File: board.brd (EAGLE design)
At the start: 126.7 x 85.7 mm, 192 parts, among them J1 XEM6310, U1 AD8022ARMZ, U2 AD5754BREZ, U3 ADR420ARZ, U4 LT1175CS8-5PBF, U5 LT1763CS8-5PBF, U6 AD5754BREZ, U7 ADR420ARZ, U8 AD8022ARMZ, U9 AD8022ARMZ, X1 LTI-SASF54GT, X10 LTI-SASF54GT, X11 LTI-SASF54GT, X12 LTI-SASF54GT, X13 LTI-SASF54GT, X14 LTI-SASF54GT, X2 LTI-SASF54GT, X3 LTI-SASF54GT, X4 LTI-SASF54GT, X5 LTI-SASF54GT, X6 LTI-SASF54GT, X7 LTI-SASF54GT, X8 LTI-SASF54GT, X9 LTI-SASF54GT

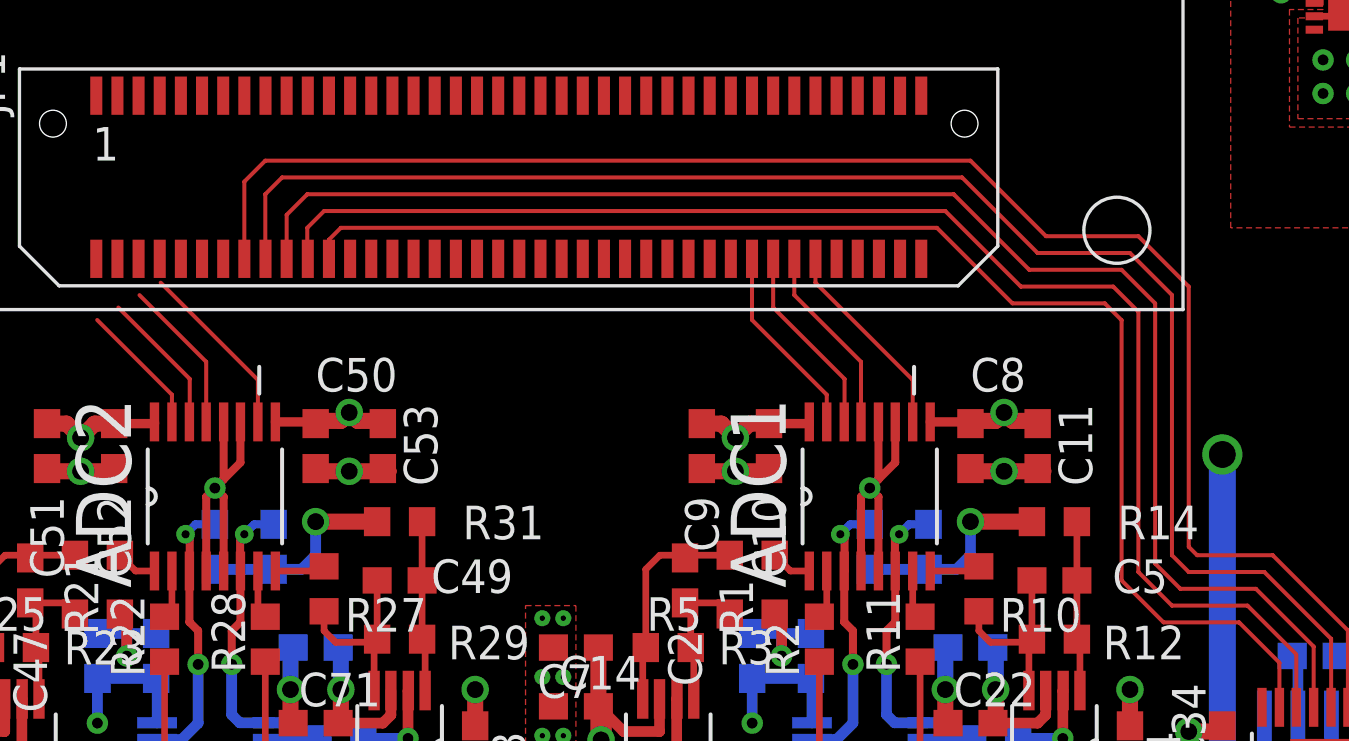
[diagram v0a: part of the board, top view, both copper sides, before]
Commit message: Board/schematic consistency
Need input wiring now
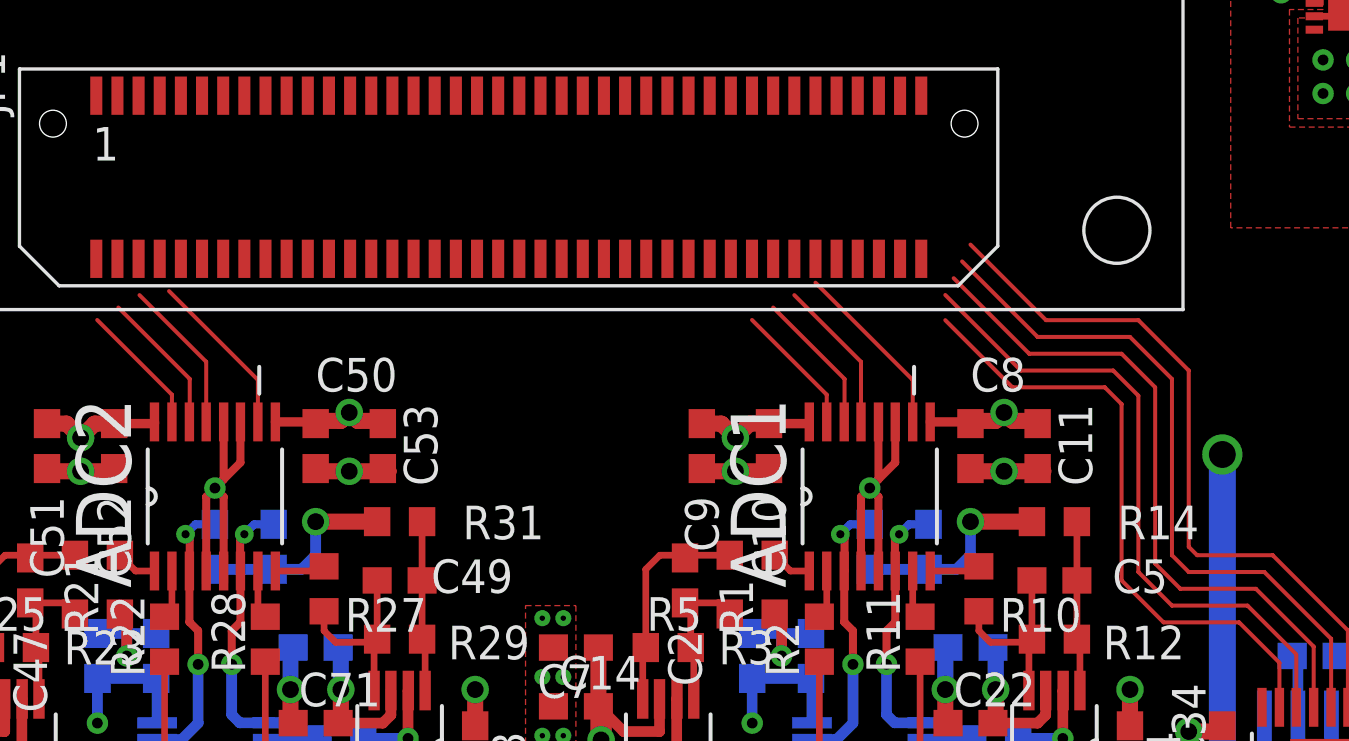
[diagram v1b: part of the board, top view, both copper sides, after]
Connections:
- net VREF1A1 renamed VREF2A
- net VREF1A2 renamed VREF3A
- net VREF1B1 renamed VREF2B
- net VREF1B2 renamed VREF3B
- removed net ADC4: J1.272
- removed net ADC5: J1.274
- removed net ADC6: J1.276
- removed net EP1: U6.25
- net ADC0: now also J1.266; no longer J1.270
- net ADC1: now also J1.264; no longer J1.268
- net ADC2: now also J1.262; no longer J1.266
- net ADC3: now also J1.260; no longer J1.264
- net DACD0: now also J1.268; no longer J1.216
- net DACD1: now also J1.270; no longer J1.218
- net DACD2: now also J1.274; no longer J1.222
- net DACD3: now also J1.272; no longer J1.220
- net DACD4: now also J1.276; no longer J1.224
- net EP: now also U6.25
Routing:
- net DACD0: track 61.0 -> 27.1 mm
- net DACD1: track 58.6 -> 26.4 mm
- net DACD3: track 56.0 -> 25.6 mm
- net DACD2: track 53.6 -> 24.8 mm
- net DACD4: track 51.1 -> 23.6 mm
- net ADC3: track 7.34 -> 5.03 mm
- net ADC2: track 7.29 -> 5.45 mm
- net ADC1: track 7.21 -> 5.84 mm
- net ADC0: track 7.69 -> 6.79 mm

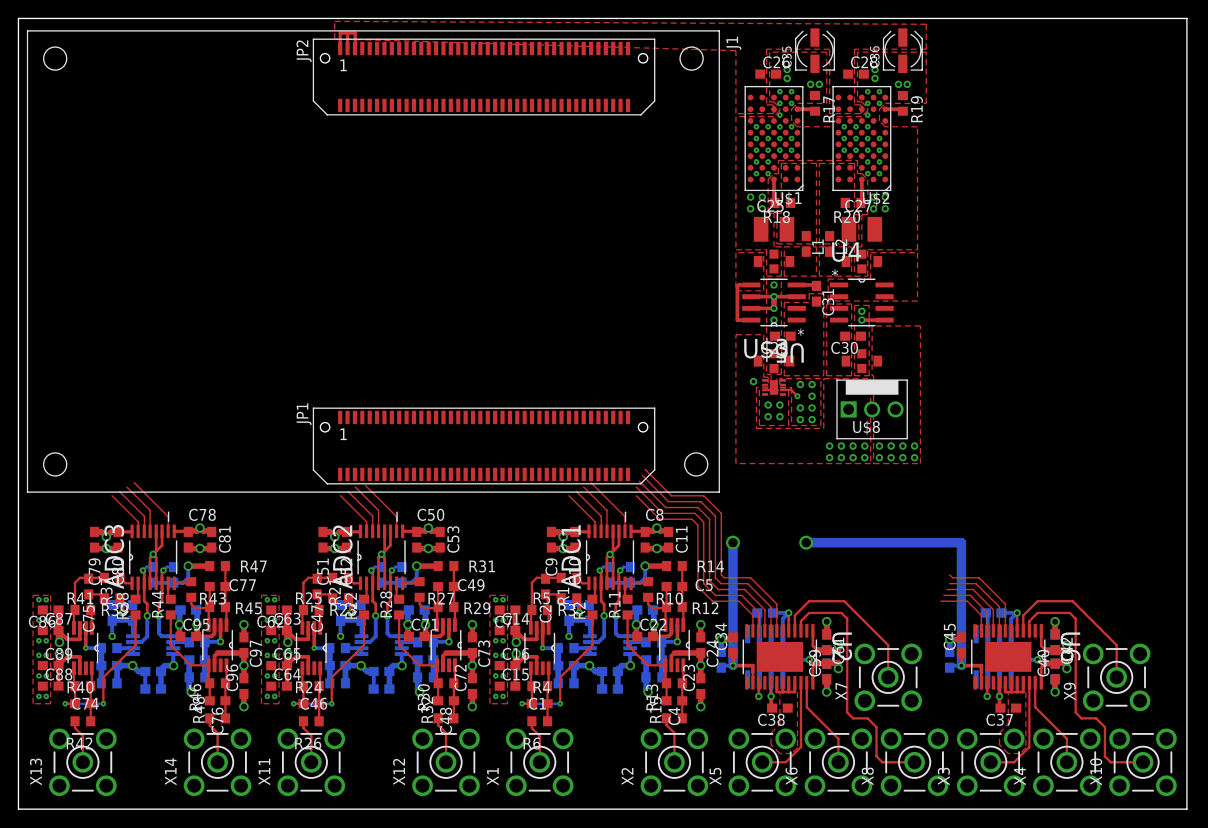
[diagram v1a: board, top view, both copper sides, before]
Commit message: Routed signals
Need to fix SMA connector spacing
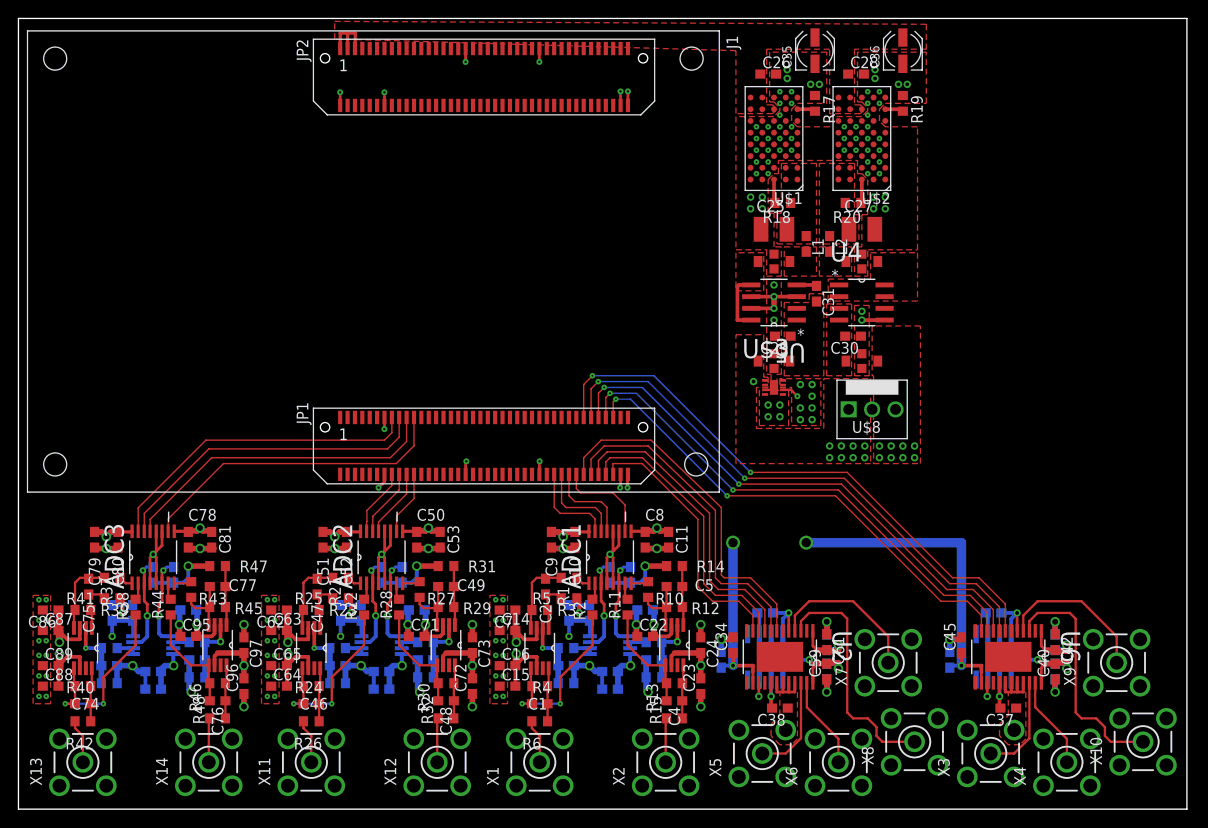
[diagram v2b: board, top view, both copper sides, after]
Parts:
- moved X10 2.22 mm to (121.9, 7.30)
- moved X8 2.22 mm to (97.2, 7.30)
- moved X7 1.59 mm to (94.3, 15.9)
- moved X9 1.59 mm to (119.1, 15.9)
- moved X14 0.95 mm to (20.6, 5.08)
- moved X2 0.95 mm to (70.2, 5.08)
- moved X3 0.95 mm to (105.4, 6.03)
- moved X5 0.95 mm to (80.6, 6.03)
- moved X12 0.95 mm to (45.4, 5.08)
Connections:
- removed net EP: U2.25, U6.25
- new net N$94: U6.25
- new net N$95: U2.25
- net ADC10: now also J1.216
- net ADC11: now also J1.221
- net ADC12: now also J1.219
- net ADC13: now also J1.217
- net ADC14: now also J1.215
- net ADC7: now also J1.222
- net ADC8: now also J1.220
- net ADC9: now also J1.218
- net DACD2: now also J1.272, U2.9; no longer J1.274, U2.10
- net DACD3: now also J1.274, U2.10; no longer J1.272, U2.9
- net DACD5: now also J1.267, U6.7; no longer U6.8
- net DACD6: now also J1.269, U6.8; no longer U6.10
- net DACD7: now also J1.271
- net DACD8: now also J1.273, U6.10; no longer U6.11
- net DACD9: now also J1.275, U6.11; no longer U6.7
- net GND: now also J1.102, J1.114, J1.135, J1.155, J1.178, J1.180, J1.213, J1.214, J1.236, J1.256, J1.278, J1.280
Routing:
- net DACD5: track 9.02 -> 62.8 mm, vias 0 -> 2
- net DACD6: track 7.47 -> 60.4 mm, vias 0 -> 2
- net DACD7: track 8.25 -> 58.0 mm, vias 0 -> 2
- net DACD8: track 6.70 -> 55.5 mm, vias 0 -> 2
- net DACD9: track 10.2 -> 53.1 mm, vias 0 -> 2
- net ADC14: track 5.03 -> 35.1 mm
- net ADC13: track 5.45 -> 35.1 mm
- net ADC12: track 5.84 -> 35.2 mm
- net ADC11: track 6.79 -> 34.4 mm
- net GND: track 197.2 -> 214.7 mm, vias 139 -> 151
- net DACD0: track 27.1 -> 38.0 mm
- net DACD1: track 26.4 -> 35.8 mm
- net DACD2: track 24.8 -> 33.5 mm
- net DACD3: track 25.6 -> 31.3 mm
- net DACD4: track 23.6 -> 29.1 mm
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
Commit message: Fixed power
Added caps for all linear regulators
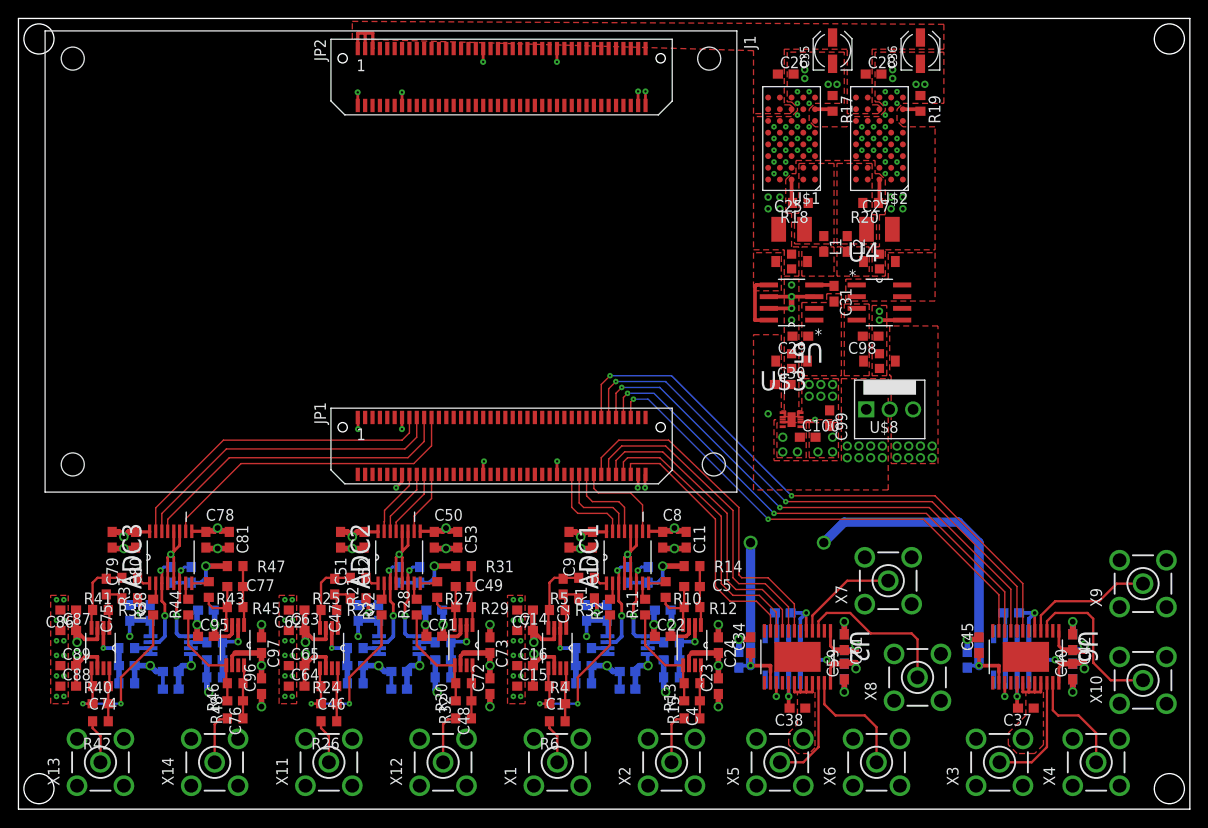
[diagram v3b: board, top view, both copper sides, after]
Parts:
- added C100, C99: 4.7uF, rcl:C0603
- added C98: 1uF Tant, rcl:C0603T
- C30: value 0.1uF Tant -> 4.7uF
- C35, C36: value (none) -> 100uF
- moved C30 9.25 mm to (82.9, 46.0), turned to 0 degrees
- moved X9 9.04 mm to (121.9, 24.4)
- moved X7 8.89 mm to (94.3, 24.8)
- moved X8 6.99 mm to (97.5, 14.3)
- moved X10 6.67 mm to (121.9, 14.0)
- moved X6 4.13 mm to (93.0, 5.08)
- moved U$3 3.98 mm to (83.8, 42.2)
- moved X4 3.17 mm to (116.8, 5.08)
- moved X5 2.13 mm to (82.5, 5.08)
- moved R2 1.91 mm to (64.1, 21.9)
- moved ADC1 1.91 mm to (66.0, 27.3)
- moved ADC2 1.91 mm to (41.3, 27.3)
- moved ADC3 1.91 mm to (16.5, 27.3)
- moved ADCOP1 1.91 mm to (58.4, 17.5)
- moved ADCOP2 1.91 mm to (73.0, 17.8)
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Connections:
- net +3V3: now also C99.1
- net +5V: now also C30.1
- net GND: now also C100.2, C30.2, C98.+, C99.2, J1.201; no longer C30.1
- net N$66: now also C98.-; no longer C30.2
- net VDD: now also C100.1
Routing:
- net N$39: track 32.4 -> 42.7 mm
- net N$21: track 26.0 -> 17.5 mm
- net N$45: track 26.0 -> 17.7 mm
- net N$18: track 16.9 -> 11.4 mm
- net N$40: track 10.8 -> 13.8 mm
- net N$28: track 1.11 -> 4.13 mm
- net S$1: track 21.2 -> 24.0 mm
- net N$19: track 10.0 -> 12.8 mm
- net N$42: track 16.9 -> 14.2 mm
- net N$36: track 10.9 -> 12.8 mm
- net S$3: track 11.1 -> 13.0 mm
- net +3V3: track 70.8 -> 72.6 mm, vias 14 -> 13
- net N$43: track 10.0 -> 11.9 mm
- net DACD6: track 60.4 -> 61.7 mm
- net DACD9: track 53.1 -> 54.4 mm
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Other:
- board size 126.7 x 85.7 mm -> 127 x 85.7 mm
- board text removed: "03/27/13"
- board text removed: "Geoffrey Ji"

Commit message: Finalized
Finished and ordered
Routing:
- net GND: vias 155 -> 156
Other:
- board text added: "Geoffrey Ji 10/31/13"
